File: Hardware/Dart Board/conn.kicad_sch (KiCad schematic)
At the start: 2 parts, among them J1 Conn_01x20_Socket, J2 Conn_01x20_Socket

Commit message: Piezo circuit
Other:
- moved on the sheet: J1, J2
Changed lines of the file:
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@@
 	)
 	(junction
-		(at 33.02 40.64)
+		(at 118.11 73.66)
 		(diameter 0)
 		(color 0 0 0 0)
 	)
 	(junction
-		(at 32.9955 43.18)
+		(at 118.0855 76.2)
 		(diameter 0)
 		(color 0 0 0 0)
@@
 	(wire
 		(pts
-			(xy 30.48 35.56) (xy 36.83 35.56)
-		)
-		(stroke
-			(width 0)
-			(type default)
-		)
-	)
-	(wire
-		(pts
-			(xy 33.02 40.64) (xy 36.83 40.64)
-		)
-		(stroke
-			(width 0)
-			(type default)
-		)
-	)
-	(wire
-		(pts
-			(xy 30.48 40.64) (xy 33.02 40.64)
-		)
-		(stroke
-			(width 0)
-			(type default)
-		)
-	)
-	(wire
-		(pts
-			(xy 32.9955 43.18) (xy 36.83 43.18)
-		)
-		(stroke
-			(width 0)
-			(type default)
-		)
-	)
-	(wire
-		(pts
-			(xy 30.48 43.18) (xy 32.9955 43.18)
-		)
-		(stroke
-			(width 0)
-			(type default)
-		)
-	)
-	(wire
-		(pts
-			(xy 30.48 38.1) (xy 36.83 38.1)
+			(xy 115.57 68.58) (xy 121.92 68.58)
+		)
+		(stroke
+			(width 0)
+			(type default)
+		)
+	)
+	(wire
+		(pts
+			(xy 118.11 73.66) (xy 121.92 73.66)
+		)
+		(stroke
+			(width 0)
+			(type default)
+		)
+	)
+	(wire
+		(pts
+			(xy 115.57 73.66) (xy 118.11 73.66)
+		)
+		(stroke
+			(width 0)
+			(type default)
+		)
+	)
+	(wire
+		(pts
+			(xy 118.0855 76.2) (xy 121.92 76.2)
+		)
+		(stroke
+			(width 0)
+			(type default)
+		)
+	)
+	(wire
+		(pts
+			(xy 115.57 76.2) (xy 118.0855 76.2)
+		)
+		(stroke
+			(width 0)
+			(type default)
+		)
+	)
+	(wire
+		(pts
+			(xy 115.57 71.12) (xy 121.92 71.12)
 		)
 		(stroke
@@
 	(global_label "GPIO_0"
 		(shape bidirectional)
-		(at 30.48 35.56 180)
+		(at 115.57 68.58 180)
 		(fields_autoplaced yes)
 		(effects
@@
 		)
 		(property "Intersheetrefs" "${INTERSHEET_REFS}"
-			(at 19.7311 35.56 0)
+			(at 104.8211 68.58 0)
 			(effects
 				(font
@@
 	(global_label "GND"
 		(shape passive)
-		(at 30.48 43.18 180)
+		(at 115.57 76.2 180)
 		(fields_autoplaced yes)
 		(effects
@@
 		)
 		(property "Intersheetrefs" "${INTERSHEET_REFS}"
-			(at 24.7356 43.18 0)
+			(at 109.8256 76.2 0)
 			(effects
 				(font
@@
 	(global_label "V_3.3"
 		(shape passive)
-		(at 30.48 40.64 180)
+		(at 115.57 73.66 180)
 		(fields_autoplaced yes)
 		(effects
@@
 		)
 		(property "Intersheetrefs" "${INTERSHEET_REFS}"
-			(at 23.5261 40.64 0)
+			(at 108.6161 73.66 0)
 			(effects
 				(font
@@
 	(global_label "GPIO_1"
 		(shape bidirectional)
-		(at 30.48 38.1 180)
+		(at 115.57 71.12 180)
 		(fields_autoplaced yes)
 		(effects
@@
 		)
 		(property "Intersheetrefs" "${INTERSHEET_REFS}"
-			(at 19.7311 38.1 0)
+			(at 104.8211 71.12 0)
 			(effects
 				(font
@@
 	(symbol
 		(lib_id "Connector:Conn_01x20_Socket")
-		(at 67.31 60.96 180)
+		(at 152.4 93.98 180)
 		(unit 1)
 		(exclude_from_sim no)
@@
 		(fields_autoplaced yes)
 		(property "Reference" "J2"
-			(at 67.945 30.48 0)
+			(at 153.035 63.5 0)
 			(effects
 				(font
@@
 		)
 		(property "Value" "Conn_01x20_Socket"
-			(at 67.945 33.02 0)
+			(at 153.035 66.04 0)
 			(effects
 				(font
@@
 		)
 		(property "Footprint" ""
-			(at 67.31 60.96 0)
+			(at 152.4 93.98 0)
 			(effects
 				(font
@@
 		)
 		(property "Datasheet" "~"
-			(at 67.31 60.96 0)
+			(at 152.4 93.98 0)
 			(effects
 				(font
@@
 		)
 		(property "Description" "Generic connector, single row, 01x20, script generated"
-			(at 67.31 60.96 0)
+			(at 152.4 93.98 0)
 			(effects
 				(font
@@
 	(symbol
 		(lib_id "power:PWR_FLAG")
-		(at 32.9955 43.18 180)
+		(at 118.0855 76.2 180)
 		(unit 1)
 		(exclude_from_sim no)
@@
 		(dnp no)
 		(property "Reference" "#FLG02"
-			(at 32.9955 45.085 0)
+			(at 118.0855 78.105 0)
 			(effects
 				(font
@@
 		)
 		(property "Value" "PWR_FLAG"
-			(at 30.48 48.26 0)
+			(at 115.57 81.28 0)
 			(effects
 				(font
@@
 		)
 		(property "Footprint" ""
-			(at 32.9955 43.18 0)
+			(at 118.0855 76.2 0)
 			(effects
 				(font
@@
 		)
 		(property "Datasheet" "~"
-			(at 32.9955 43.18 0)
+			(at 118.0855 76.2 0)
 			(effects
 				(font
@@
 		)
 		(property "Description" "Special symbol for telling ERC where power comes from"
-			(at 32.9955 43.18 0)
+			(at 118.0855 76.2 0)
 			(effects
 				(font
@@
 	(symbol
 		(lib_id "power:PWR_FLAG")
-		(at 33.02 40.64 0)
+		(at 118.11 73.66 0)
 		(unit 1)
 		(exclude_from_sim no)
@@
 		(dnp no)
 		(property "Reference" "#FLG01"
-			(at 33.02 38.735 0)
+			(at 118.11 71.755 0)
 			(effects
 				(font
@@
 		)
 		(property "Value" "PWR_FLAG"
-			(at 18.796 40.64 0)
+			(at 103.886 73.66 0)
 			(effects
 				(font
@@
 		)
 		(property "Footprint" ""
-			(at 33.02 40.64 0)
+			(at 118.11 73.66 0)
 			(effects
 				(font
@@
 		)
 		(property "Datasheet" "~"
-			(at 33.02 40.64 0)
+			(at 118.11 73.66 0)
 			(effects
 				(font
@@
 		)
 		(property "Description" "Special symbol for telling ERC where power comes from"
-			(at 33.02 40.64 0)
+			(at 118.11 73.66 0)
 			(effects
 				(font
@@
 	(symbol
 		(lib_id "Connector:Conn_01x20_Socket")
-		(at 41.91 58.42 0)
+		(at 127 91.44 0)
 		(unit 1)
 		(exclude_from_sim no)
@@
 		(dnp no)
 		(property "Reference" "J1"
-			(at 33.02 28.702 0)
+			(at 118.11 61.722 0)
 			(effects
 				(font
@@
 		)
 		(property "Value" "Conn_01x20_Socket"
-			(at 33.02 31.242 0)
+			(at 118.11 64.262 0)
 			(effects
 				(font
@@
 		)
 		(property "Footprint" ""
-			(at 41.91 58.42 0)
+			(at 127 91.44 0)
 			(effects
 				(font
@@
 		)
 		(property "Datasheet" "~"
-			(at 41.91 58.42 0)
+			(at 127 91.44 0)
 			(effects
 				(font
@@
 		)
 		(property "Description" "Generic connector, single row, 01x20, script generated"
-			(at 41.91 58.42 0)
-			(effects
-				(font
+			(at 127 91.44 0)
+			(effects
+				(font

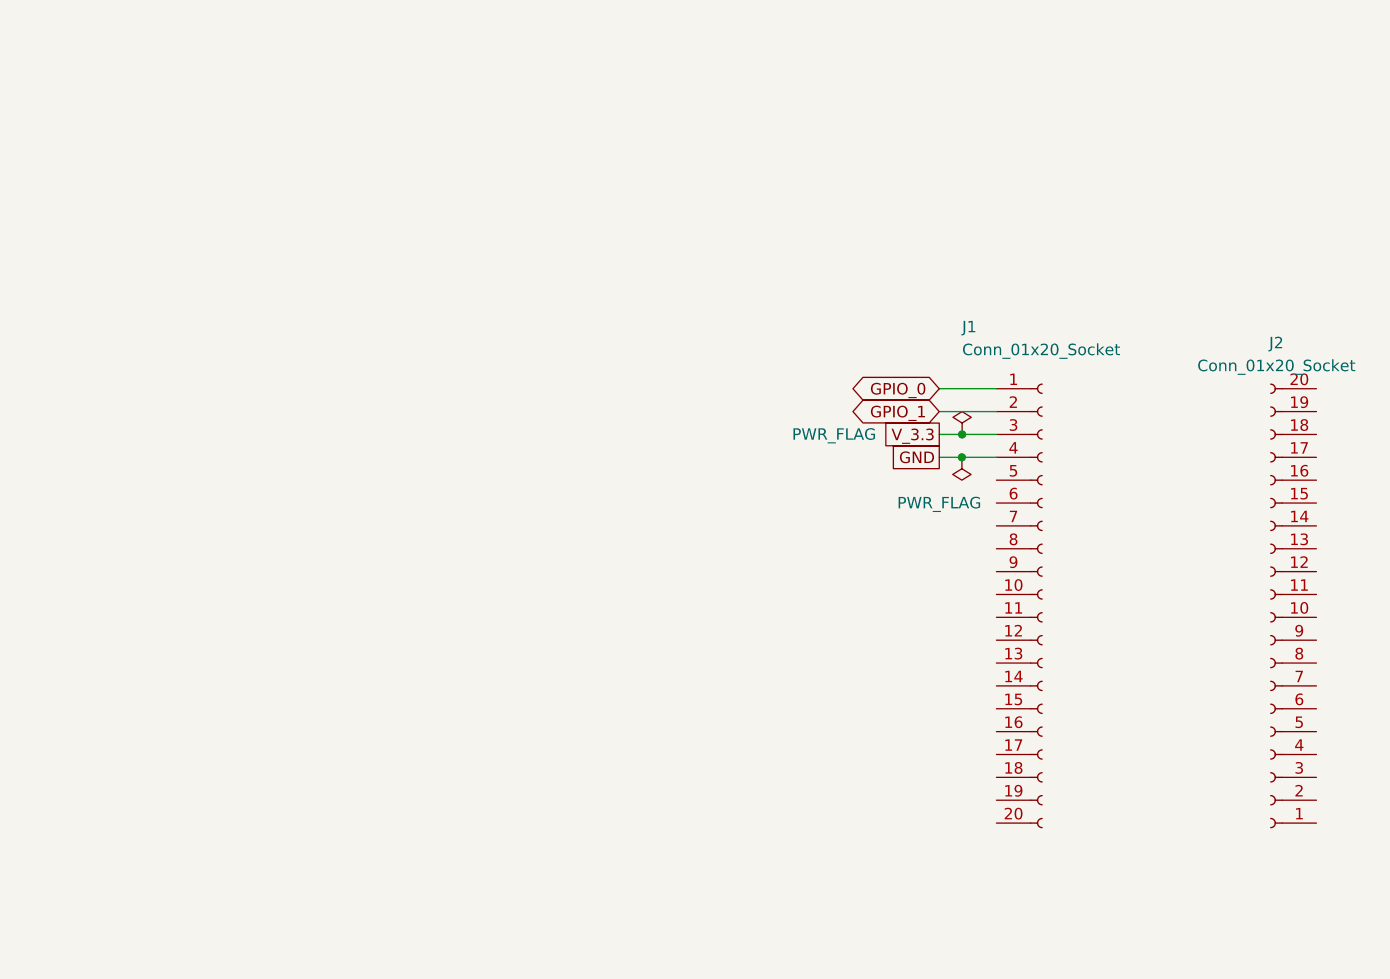
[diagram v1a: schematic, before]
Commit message: Assigned Footprints and added to PCB editor
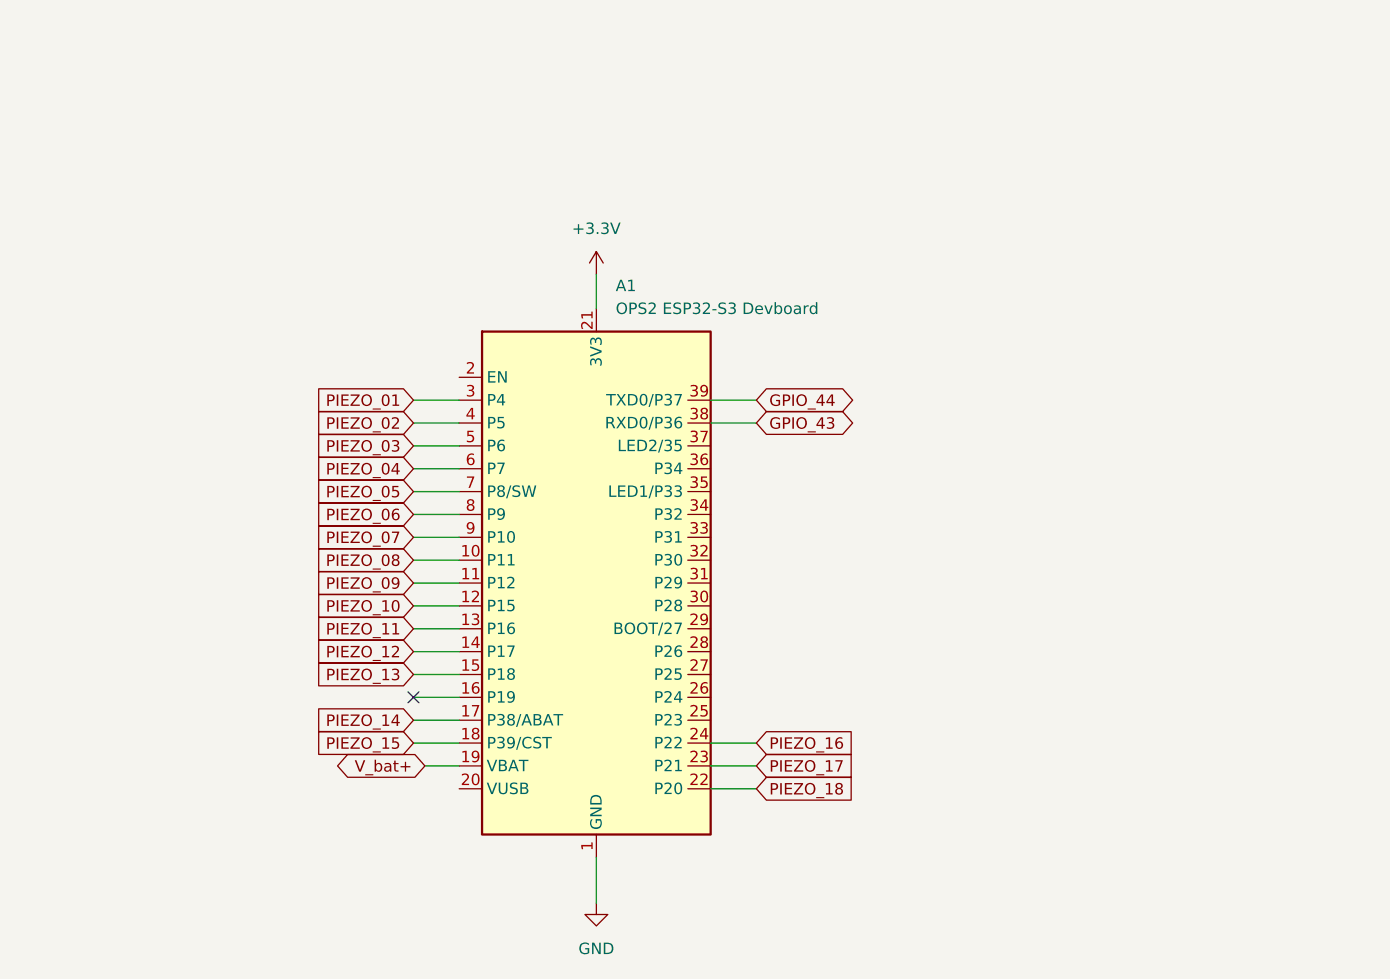
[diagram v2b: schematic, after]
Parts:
- removed J1, J2: Conn_01x20_Socket, symbol Connector:Conn_01x20_Socket
- added A1: OPS2 ESP32-S3 Devboard, IEEE_OPS2:ESP32_Devboard, symbol IEEE_OPS2:ESP32_Devboard
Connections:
- net GND: now also A1.1 (GND), A1.40 (GND)
- new net +3.3V: A1.21 (3V3)
- new net GPIO_43: A1.38 (RXD0/P36)
- new net GPIO_44: A1.39 (TXD0/P37)
- new net PIEZO_01: A1.3 (P4)
- new net PIEZO_02: A1.4 (P5)
- new net PIEZO_03: A1.5 (P6)
- new net PIEZO_04: A1.6 (P7)
- new net PIEZO_05: A1.7 (P8/SW)
- new net PIEZO_06: A1.8 (P9)
- new net PIEZO_07: A1.9 (P10)
- new net PIEZO_08: A1.10 (P11)
- new net PIEZO_09: A1.11 (P12)
- new net PIEZO_10: A1.12 (P15)
- new net PIEZO_11: A1.13 (P16)
- new net PIEZO_12: A1.14 (P17)
- new net PIEZO_13: A1.15 (P18)
- new net PIEZO_14: A1.17 (P38/ABAT)
- new net PIEZO_15: A1.18 (P39/CST)
- new net PIEZO_16: A1.24 (P22)
- new net PIEZO_17: A1.23 (P21)
- new net PIEZO_18: A1.22 (P20)
- new net V_bat+: A1.19 (VBAT)
- no-connect marks 0 -> 1

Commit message: Finished PCB Layout
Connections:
- net GPIO_43: now also A1.33 (P31); no longer A1.38 (RXD0/P36)
- net GPIO_44: now also A1.34 (P32); no longer A1.39 (TXD0/P37)
- net PIEZO_11: now also A1.14 (P17); no longer A1.13 (P16)
- net PIEZO_12: now also A1.15 (P18); no longer A1.14 (P17)
- net PIEZO_13: now also A1.16 (P19); no longer A1.15 (P18)
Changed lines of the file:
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@@
 	)
 	(no_connect
-		(at 57.15 102.87)
+		(at 57.15 95.25)
 	)
 	(wire
@@
 	(wire
 		(pts
-			(xy 90.17 69.85) (xy 95.25 69.85)
+			(xy 90.17 82.55) (xy 95.25 82.55)
 		)
 		(stroke
@@
 	(wire
 		(pts
-			(xy 90.17 72.39) (xy 95.25 72.39)
+			(xy 90.17 85.09) (xy 95.25 85.09)
 		)
 		(stroke
@@
 	(global_label "PIEZO_12"
 		(shape input)
-		(at 57.15 97.79 180)
-		(fields_autoplaced yes)
-		(effects
-			(font
-				(size 1.27 1.27)
-			)
-			(justify right)
-		)
-		(property "Intersheetrefs" "${INTERSHEET_REFS}"
-			(at 45.2144 97.79 0)
+		(at 57.15 100.33 180)
+		(fields_autoplaced yes)
+		(effects
+			(font
+				(size 1.27 1.27)
+			)
+			(justify right)
+		)
+		(property "Intersheetrefs" "${INTERSHEET_REFS}"
+			(at 45.2144 100.33 0)
 			(effects
 				(font
@@
 	(global_label "PIEZO_13"
 		(shape input)
-		(at 57.15 100.33 180)
-		(fields_autoplaced yes)
-		(effects
-			(font
-				(size 1.27 1.27)
-			)
-			(justify right)
-		)
-		(property "Intersheetrefs" "${INTERSHEET_REFS}"
-			(at 45.2144 100.33 0)
+		(at 57.15 102.87 180)
+		(fields_autoplaced yes)
+		(effects
+			(font
+				(size 1.27 1.27)
+			)
+			(justify right)
+		)
+		(property "Intersheetrefs" "${INTERSHEET_REFS}"
+			(at 45.2144 102.87 0)
 			(effects
 				(font
@@
 	(global_label "GPIO_43"
 		(shape bidirectional)
-		(at 95.25 72.39 0)
+		(at 95.25 85.09 0)
 		(fields_autoplaced yes)
 		(effects
@@
 		)
 		(property "Intersheetrefs" "${INTERSHEET_REFS}"
-			(at 107.2084 72.39 0)
+			(at 107.2084 85.09 0)
 			(effects
 				(font
@@
 	(global_label "PIEZO_11"
 		(shape input)
-		(at 57.15 95.25 180)
-		(fields_autoplaced yes)
-		(effects
-			(font
-				(size 1.27 1.27)
-			)
-			(justify right)
-		)
-		(property "Intersheetrefs" "${INTERSHEET_REFS}"
-			(at 45.2144 95.25 0)
+		(at 57.15 97.79 180)
+		(fields_autoplaced yes)
+		(effects
+			(font
+				(size 1.27 1.27)
+			)
+			(justify right)
+		)
+		(property "Intersheetrefs" "${INTERSHEET_REFS}"
+			(at 45.2144 97.79 0)
 			(effects
 				(font
@@
 	(global_label "GPIO_44"
 		(shape bidirectional)
-		(at 95.25 69.85 0)
+		(at 95.25 82.55 0)
 		(fields_autoplaced yes)
 		(effects
@@
 		)
 		(property "Intersheetrefs" "${INTERSHEET_REFS}"
-			(at 107.2084 69.85 0)
-			(effects
-				(font
+			(at 107.2084 82.55 0)
+			(effects
+				(font
